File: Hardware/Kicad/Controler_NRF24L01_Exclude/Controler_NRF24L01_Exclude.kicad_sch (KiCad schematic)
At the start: 51 parts, among them J1 Conn_01x02, SW1 SW_Push, SW10 SW_Push, SW11 SW_DIP_x01, SW12 SW_Push, SW13 SW_DIP_x01, SW2 SW_Push, SW3 SW_Push, SW4 SW_Push, SW5 SW_Push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

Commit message: correction
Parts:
- removed D7: D_Small, Diode_SMD:D_0603_1608Metric_Pad1.05x0.95mm_HandSolder, symbol Device:D_Small
- added C1: 100uF, symbol Device:C_Polarized
- added J2: Conn_02x07_Odd_Even, Connector_PinHeader_1.27mm:PinHeader_2x07_P1.27mm_Vertical_SMD, symbol Connector_Generic:Conn_02x07_Odd_Even
- added R2: R_Small, symbol Device:R_Small
- C11: value C_Small -> 470p
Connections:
- net +3V8: no longer C12.1, C13.1, R14.1, R15.1, R16.1, R17.1, SW11.1
- net GND: now also C1.2, J2.11 (Pin_11), J2.5 (Pin_5), J2.7 (Pin_7), R2.2
- net Glob_Alim: now also D1.2 (A), U1.1 (VDD), U1.17 (VDD), U1.5 (VDDA), U2.3 (OUT), C1.1; no longer D1.1 (K)
- net NES/SNES_switcher: now also U1.15 (PB1); no longer U1.23 (PA13)
- net X_Button: now also U1.3 (PC15); no longer U1.8 (PA2)
- net Y_Button: now also U1.2 (PC14); no longer U1.9 (PA3)
- net SWDCK: now reaches U1.24 (PA14)
- net SWDCK: now also J2.6 (Pin_6)
- net NRST: now reaches U1.4 (NRST)
- new net: D1.1 (K), R2.1
- new net +3.3V: J2.3 (Pin_3)
- new net Li-ion: C12.1, C13.1, R14.1, R15.1, R16.1, R17.1, SW11.1
- new net Reset_Buton : J2.12 (Pin_12)
- new net SWDIO: J2.4 (Pin_4), U1.23 (PA13)
- new net USART2_RX: J2.13 (Pin_13), U1.9 (PA3)
- new net USART2_TX: J2.14 (Pin_14), U1.8 (PA2)
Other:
- note added: "DC/DC convertor Input : 4.2V"
- note added: "SWD Connector"
- note removed: "DC/DC convertor"

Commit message: Maybe the final version
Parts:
- removed C12: 1nF, Capacitor_SMD:C_0603_1608Metric_Pad1.08x0.95mm_HandSolder, symbol Device:C_Small
- removed D2, D3, D4, D5, D6: LED, LED_SMD:LED_0603_1608Metric_Pad1.05x0.95mm_HandSolder, symbol Device:LED
- removed R13, R18: 1K, Resistor_SMD:R_0603_1608Metric_Pad0.98x0.95mm_HandSolder, symbol Device:R_Small
- removed R14, R15, R16, R17: R_Small, Resistor_SMD:R_0603_1608Metric_Pad0.98x0.95mm_HandSolder, symbol Device:R_Small
- removed R2: R_Small, symbol Device:R_Small
- removed SW12: SW_Push, Button_Switch_THT:SW_PUSH_6mm_H5mm, symbol Switch:SW_Push
- added R4, R5: 1K, Resistor_SMD:R_0603_1608Metric_Pad0.98x0.95mm_HandSolder, symbol Device:R_Small
- added SW7: SW_SPST, Button_Switch_SMD:SW_SPST_B3S-1000, symbol Switch:SW_SPST
- added TP1: R, Connector_Coaxial:SMA_Molex_73251-1153_EdgeMount_Horizontal, symbol Connector:CoaxialSwitch_Testpoint
- added TP2: L, Connector_Coaxial:SMA_Molex_73251-1153_EdgeMount_Horizontal, symbol Connector:CoaxialSwitch_Testpoint
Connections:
- net GND: now also R4.2, R5.2, SW7.1 (A), TP1.G, TP2.G
- net Glob_Alim: now also D1.1 (K), TP1.C, TP2.C; no longer D1.2 (A), U2.3 (OUT)
- net Order_Search: now also SW7.2 (B)
- new net: D1.2 (A), U2.3 (OUT)
- new net L: R5.1, TP2.A
- new net R: R4.1, TP1.A
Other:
- added sheet Diode (Diode.kicad_sch)
- note added: "L/R switcher"
- note added: "SWITCH NES/SNES"
- note removed: "ENERGY LEVEL"
- moved on the sheet: D1

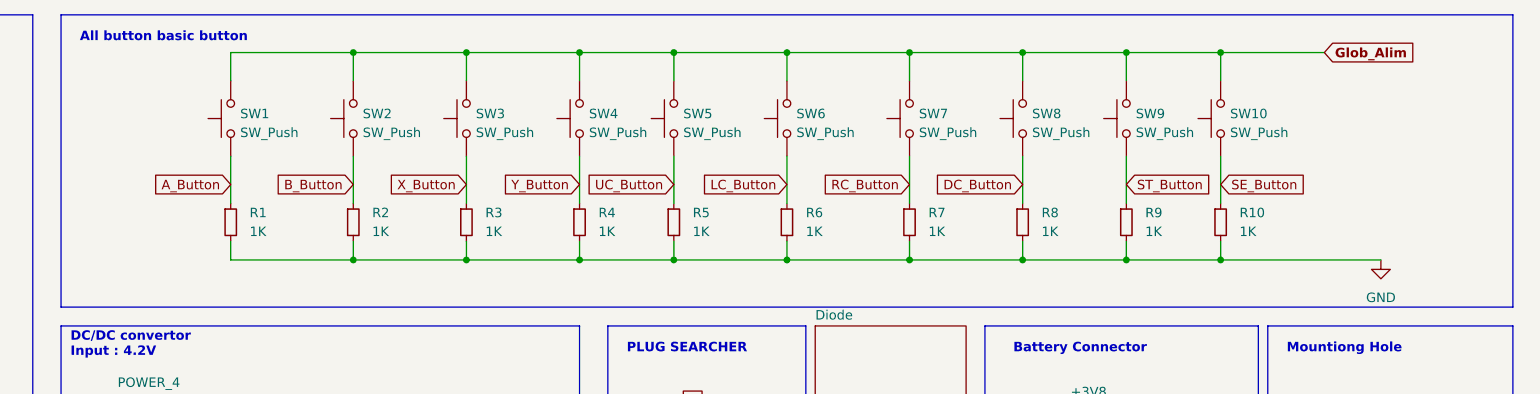
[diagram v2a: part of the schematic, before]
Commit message: Exculde Time
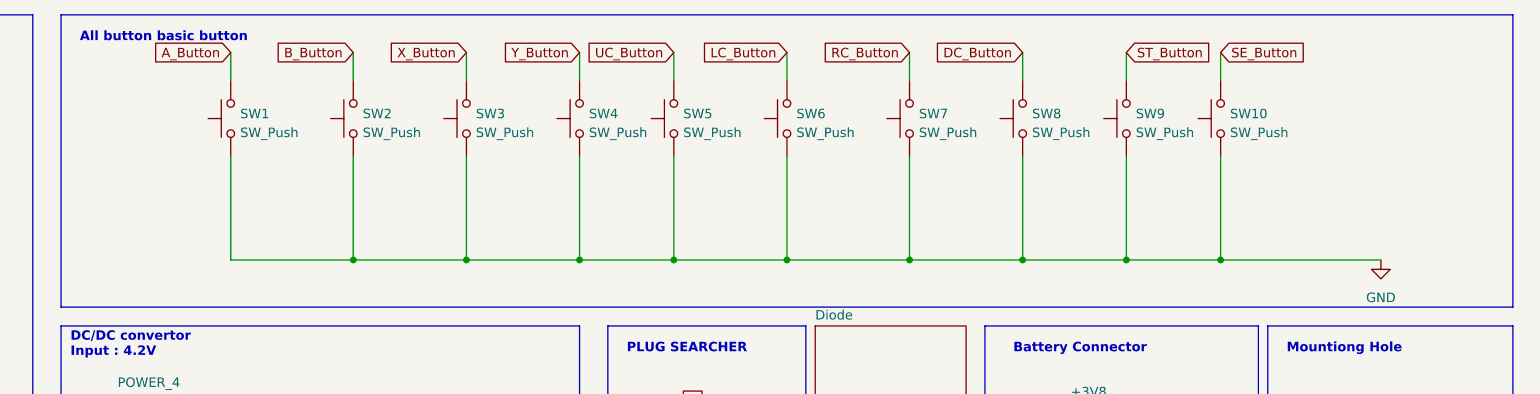
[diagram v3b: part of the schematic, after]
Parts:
- removed R1, R10, R2, R3, R4, R5, R6, R7, R8, R9: 1K, Resistor_SMD:R_0603_1608Metric_Pad0.98x0.95mm_HandSolder, symbol Device:R_Small
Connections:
- net A_Button: now also SW1.2; no longer SW1.1
- net B_Button: now also SW2.2; no longer SW2.1
- net DC_Button: now also SW8.2; no longer SW8.1
- net GND: now also SW1.1, SW10.1, SW2.1, SW3.1, SW4.1, SW5.1, SW6.1, SW7.1, SW8.1, SW9.1
- net Glob_Alim: no longer SW1.2, SW10.2, SW2.2, SW3.2, SW4.2, SW5.2, SW6.2, SW7.2, SW8.2, SW9.2
- net LC_Button: now also SW6.2; no longer SW6.1
- net RC_Button: now also SW7.2; no longer SW7.1
- net SE_Button: now also SW10.2; no longer SW10.1
- net ST_Button: now also SW9.2; no longer SW9.1
- net UC_Button: now also SW5.2; no longer SW5.1
- net X_Button: now also SW3.2; no longer SW3.1
- net Y_Button: now also SW4.2; no longer SW4.1

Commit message: Exculde finish
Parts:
- added D3: D_Small, LED_SMD:LED_0603_1608Metric_Pad1.05x0.95mm_HandSolder, symbol Device:D_Small
- SW1, SW10, SW2, SW3, SW4, SW5, SW6, SW7, SW8, SW9: footprint Button_Switch_THT:SW_PUSH_6mm_H5mm -> Button_Switch_SMD:SW_SPST_B3S-1000
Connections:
- net LED_Order is gone; now on net Y_Button: U1.22 (PA12)
- net Li-ion is gone; now on net +3V8: C13.1, SW11.1
- net NRST is gone; now on net Reset_Buton : U1.4 (NRST)
- net DC_Button: now also U1.14 (PB0); no longer U1.11 (PA5)
- net Digital_Out_Put: now also U1.12 (PA6); no longer U1.27 (PB4)
- net Glob_Alim: now also D3.2 (A); no longer U1.1 (VDD), U1.17 (VDD), U1.5 (VDDA)
- net L: now also U1.30 (PB7)
- net LC_Button: now also U1.3 (PC15); no longer U1.12 (PA6)
- net MOSI: now also U1.13 (PA7); no longer U1.28 (PB5)
- net NES/SNES_switcher: now also U1.31 (PH3); no longer U1.15 (PB1)
- net Order_Search: now also U1.10 (PA4); no longer U1.20 (PA10)
- net Pin_Clock: now also U1.11 (PA5); no longer U1.26 (PB3)
- net R: now also U1.29 (PB6)
- net RC_Button: now also U1.2 (PC14); no longer U1.13 (PA7)
- net UC_Button: now also U1.15 (PB1); no longer U1.10 (PA4)
- net X_Button: now also U1.20 (PA10); no longer U1.3 (PC15)
- net Y_Button: no longer U1.2 (PC14)
- new net: D3.1 (K), U1.1 (VDD), U1.17 (VDD), U1.5 (VDDA)
- new net DIODE_CLK: U1.26 (PB3)
- new net DIODE_SDA: U1.28 (PB5)
- new net POWER_CHECK: U1.27 (PB4)
- no-connect marks 13 -> 9
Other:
- moved on the sheet: U1

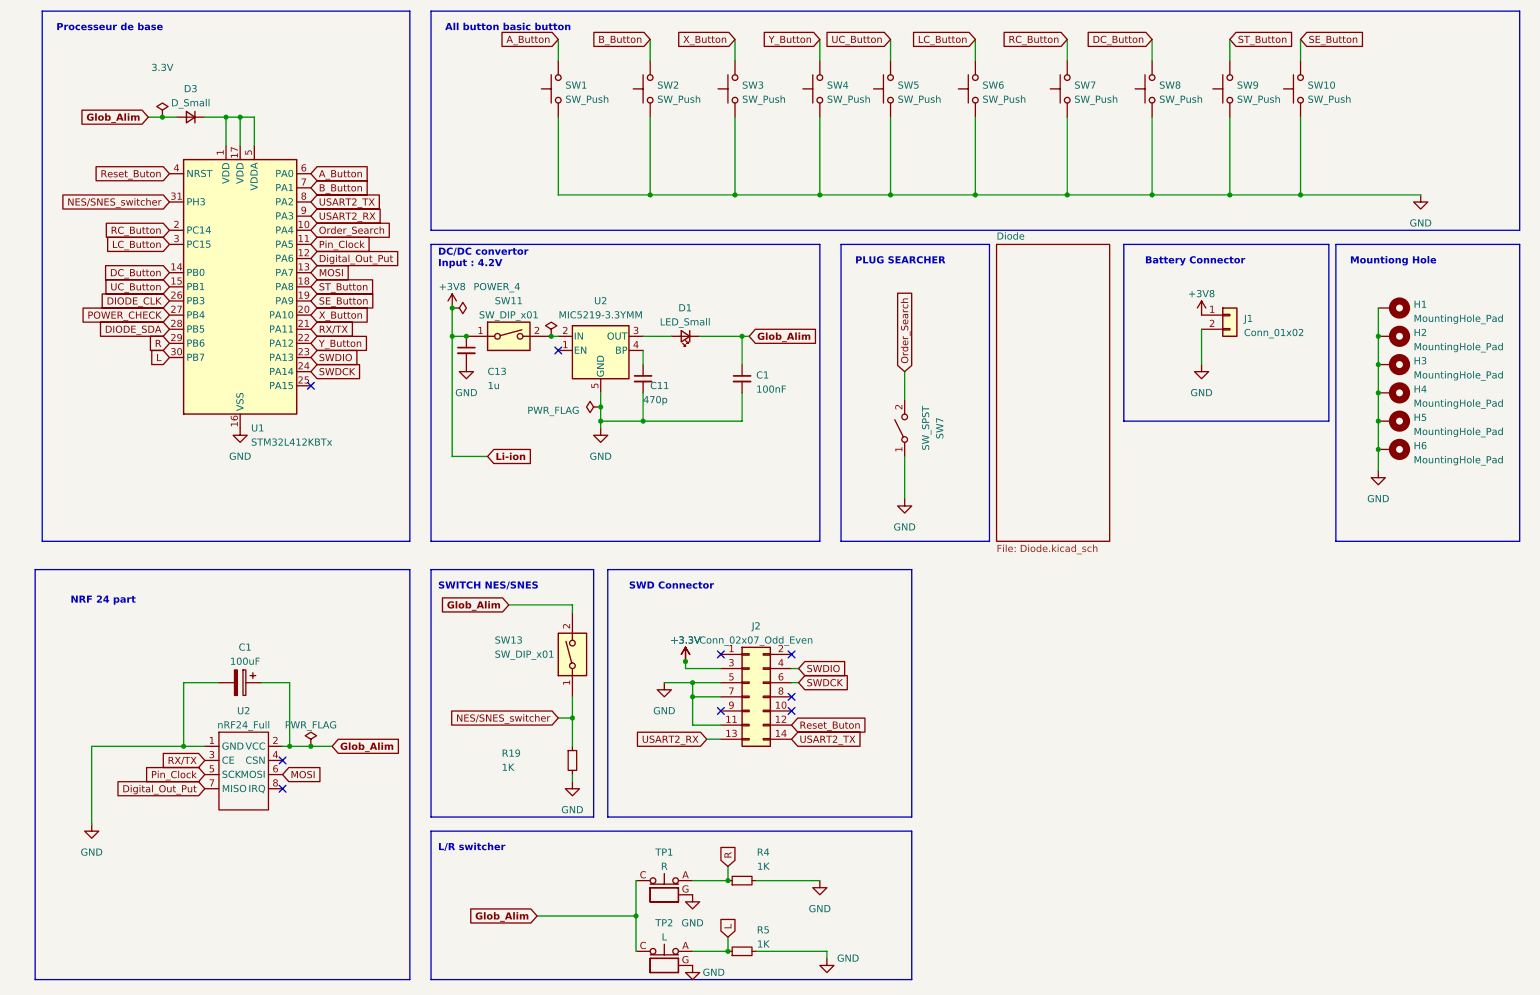
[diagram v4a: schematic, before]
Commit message: update of the folder 'controler_NRF24L01_Exclude' -> replace by the correction given
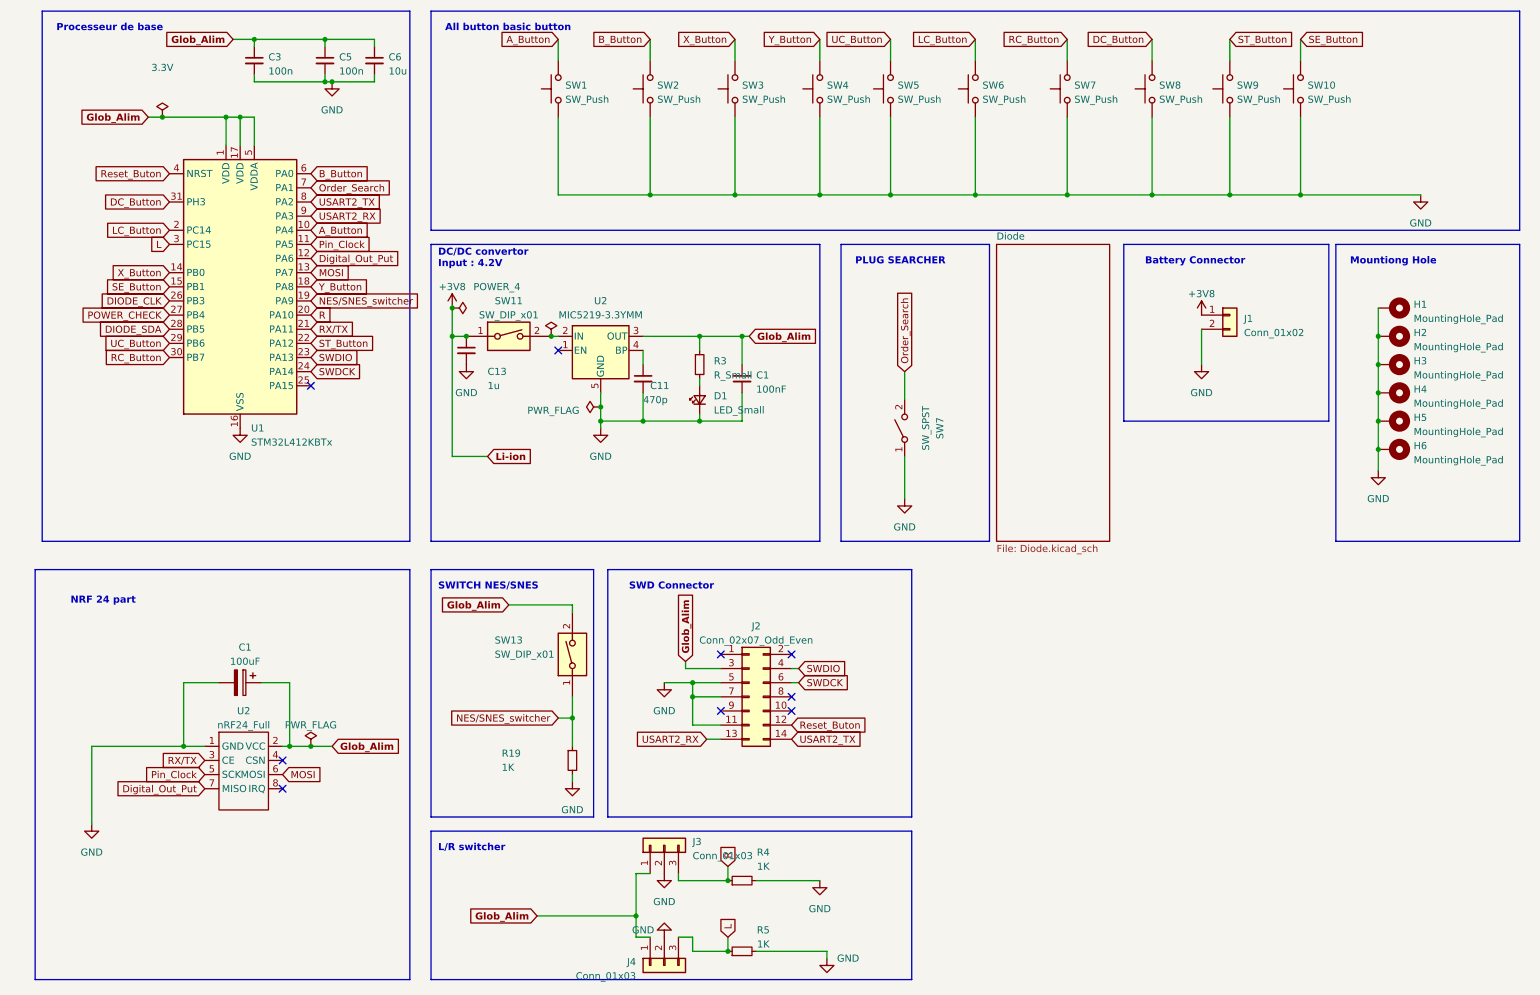
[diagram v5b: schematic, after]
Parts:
- removed D3: D_Small, LED_SMD:LED_0603_1608Metric_Pad1.05x0.95mm_HandSolder, symbol Device:D_Small
- removed TP1: R, Connector_Coaxial:SMA_Molex_73251-1153_EdgeMount_Horizontal, symbol Connector:CoaxialSwitch_Testpoint
- removed TP2: L, Connector_Coaxial:SMA_Molex_73251-1153_EdgeMount_Horizontal, symbol Connector:CoaxialSwitch_Testpoint
- added C3, C5: 100n, Resistor_SMD:R_0603_1608Metric_Pad0.98x0.95mm_HandSolder, symbol Device:C_Small
- added C6: 10u, Resistor_SMD:R_0603_1608Metric_Pad0.98x0.95mm_HandSolder, symbol Device:C_Small
- added J3, J4: Conn_01x03, Connector_JST:JST_XH_B3B-XH-A_1x03_P2.50mm_Vertical, symbol Connector_Generic:Conn_01x03
- added R3: R_Small, Resistor_SMD:R_0603_1608Metric_Pad0.98x0.95mm_HandSolder, symbol Device:R_Small
- C1: footprint (none) -> Capacitor_SMD:CP_Elec_5x5.4
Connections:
- net +3.3V is gone; now on net Glob_Alim: J2.3 (Pin_3)
- net A_Button: now also U1.10 (PA4); no longer U1.6 (PA0)
- net B_Button: now also U1.6 (PA0); no longer U1.7 (PA1)
- net DC_Button: now also U1.31 (PH3); no longer U1.14 (PB0)
- net GND: now also D1.1 (K), C3.2, C5.2, C6.2, J3.2 (Pin_2), J4.2 (Pin_2)
- net Glob_Alim: now also U1.1 (VDD), U1.17 (VDD), U1.5 (VDDA), U2.3 (OUT), C3.1, C5.1, C6.1, J3.1 (Pin_1), J4.1 (Pin_1), R3.1; no longer D1.1 (K)
- net L: now also U1.3 (PC15), J4.3 (Pin_3); no longer U1.30 (PB7)
- net LC_Button: now also U1.2 (PC14); no longer U1.3 (PC15)
- net NES/SNES_switcher: now also U1.19 (PA9); no longer U1.31 (PH3)
- net Order_Search: now also U1.7 (PA1); no longer U1.10 (PA4)
- net R: now also U1.20 (PA10), J3.3 (Pin_3); no longer U1.29 (PB6)
- net RC_Button: now also U1.30 (PB7); no longer U1.2 (PC14)
- net SE_Button: now also U1.15 (PB1); no longer U1.19 (PA9)
- net ST_Button: now also U1.22 (PA12); no longer U1.18 (PA8)
- net UC_Button: now also U1.29 (PB6); no longer U1.15 (PB1)
- net X_Button: now also U1.14 (PB0); no longer U1.20 (PA10)
- net Y_Button: now also U1.18 (PA8); no longer U1.22 (PA12)
- net at D1.2 (A): now also R3.2; no longer U2.3 (OUT)

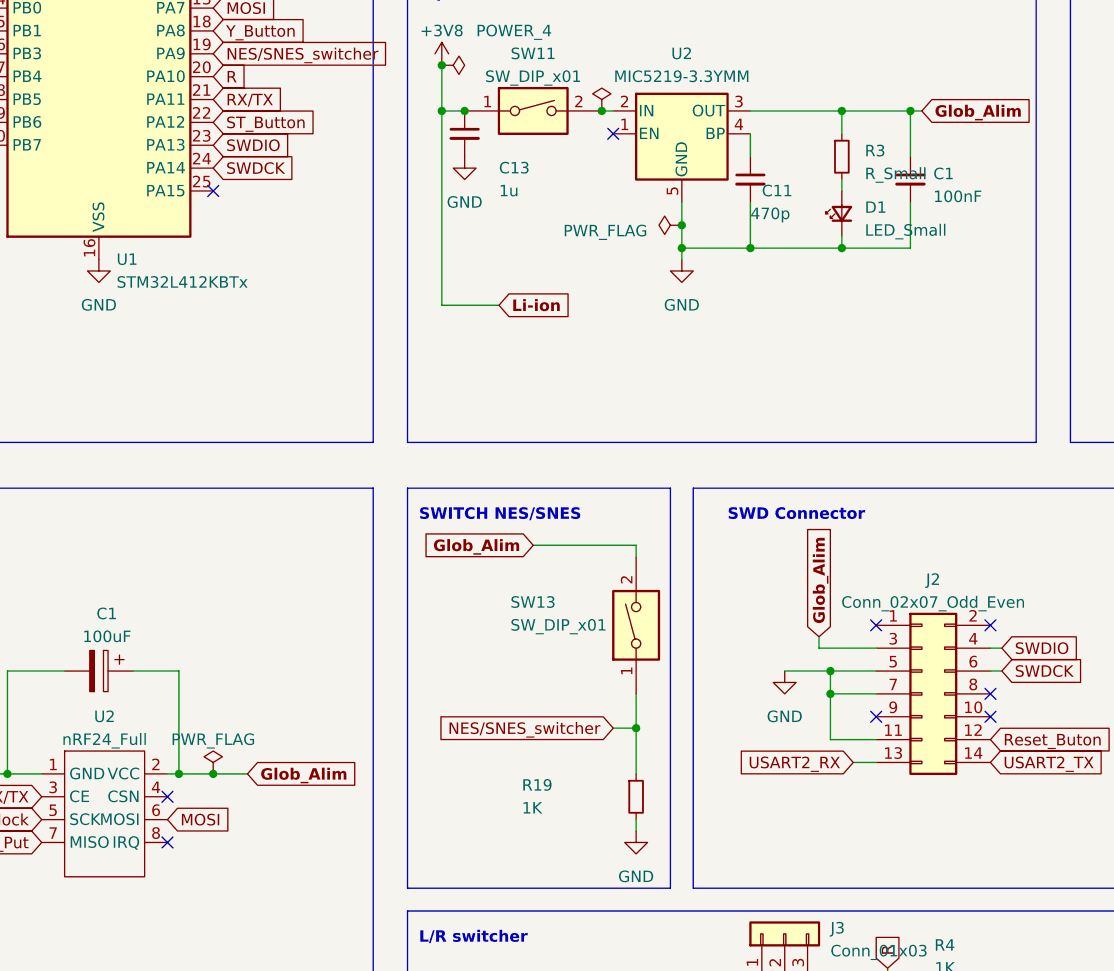
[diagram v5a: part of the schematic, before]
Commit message: Updated Plug_NRF24L01_Exclude (Ground vias)
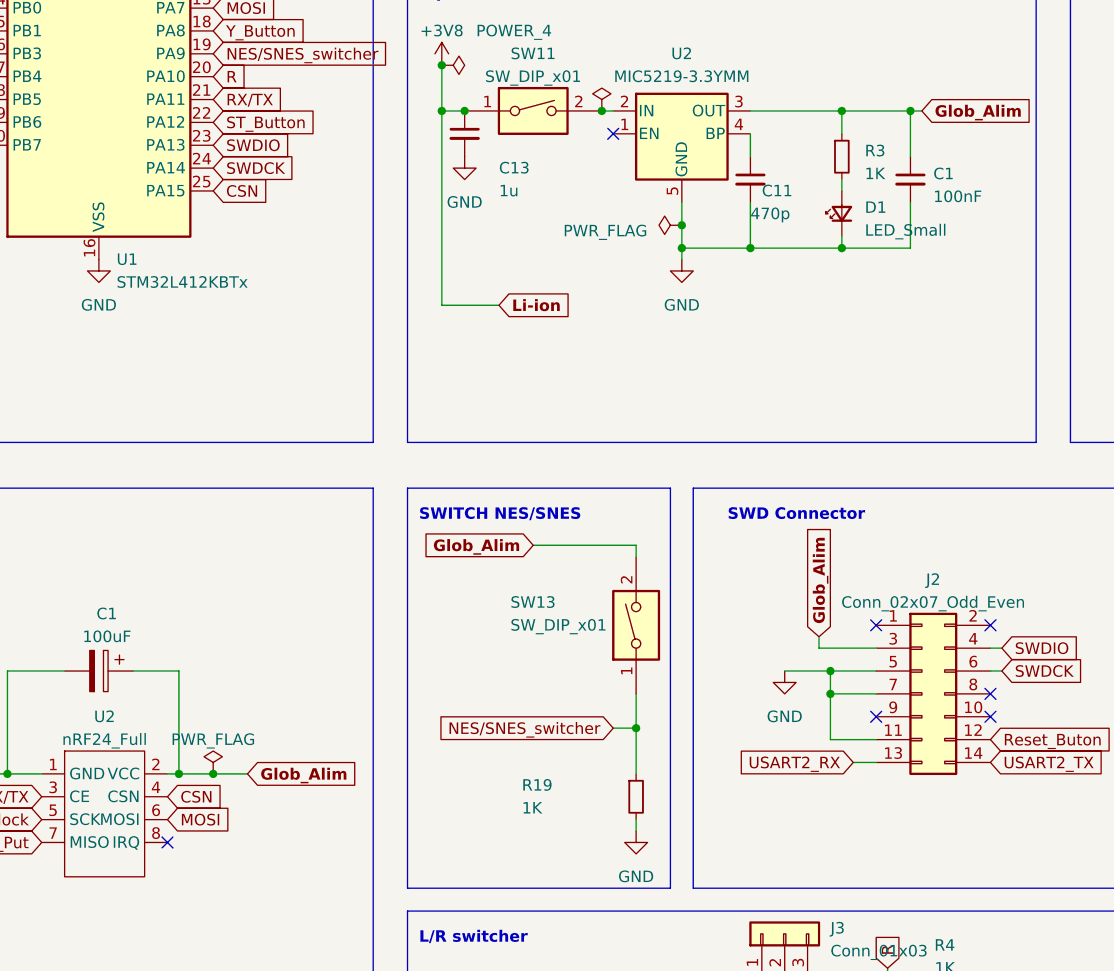
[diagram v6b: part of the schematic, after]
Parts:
- R3: value R_Small -> 1K
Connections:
- net CSN: now reaches U2.4 (CSN)
- net CSN: now also U1.25 (PA15)
- no-connect marks 9 -> 7
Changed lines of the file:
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@@
   (no_connect (at 107.95 76.2))
   (no_connect (at 149.86 138.43))
-  (no_connect (at 63.5 82.55))
   (no_connect (at 149.86 140.97))
   (no_connect (at 137.16 140.97))
@@
   (no_connect (at 58.42 154.94))
   (no_connect (at 137.16 130.81))
-  (no_connect (at 58.42 149.86))
   (polyline (pts (xy 15.24 110.49) (xy 81.28 110.49))
     (stroke (width 0) (type default))
@@
     )
   )
+  (global_label "CSN" (shape input) (at 63.5 82.55 0) (fields_autoplaced)
+    (effects (font (size 1.27 1.27)) (justify left))
+    (property "Intersheetrefs" "${INTERSHEET_REFS}" (at 70.2158 82.55 0)
+      (effects (font (size 1.27 1.27)) (justify left) hide)
+    )
+  )
   (global_label "Glob_Alim" (shape input) (at 34.29 34.29 180) (fields_autoplaced)
     (effects (font (size 1.27 1.27) bold) (justify right))
@@
     (property "Intersheetrefs" "${INTERSHEET_REFS}" (at 186.8082 20.32 0)
       (effects (font (size 1.27 1.27)) (justify right) hide)
+    )
+  )
+  (global_label "CSN" (shape input) (at 58.42 149.86 0) (fields_autoplaced)
+    (effects (font (size 1.27 1.27)) (justify left))
+    (property "Intersheetrefs" "${INTERSHEET_REFS}" (at 65.1358 149.86 0)
+      (effects (font (size 1.27 1.27)) (justify left) hide)
     )
   )
@@
       (effects (font (size 1.27 1.27)) (justify left))
     )
-    (property "Value" "R_Small" (at 135.89 80.645 0)
+    (property "Value" "1K" (at 135.89 80.645 0)
       (effects (font (size 1.27 1.27)) (justify left))
     )
